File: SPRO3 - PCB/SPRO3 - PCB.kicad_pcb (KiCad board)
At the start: 2 copper layers, 100 x 100 mm, 39 parts, among them J1 Power Input, J10 Conn_01x03_Pin, J11 Conn_01x03_Pin, J12 Conn_01x03_Pin, J13 Conn_01x03_Pin, J14 Conn_01x03_Pin, J15 Conn_01x03_Pin, J16 Spare I2C PINS, J2 2nd PCB, J3 Servo Motor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

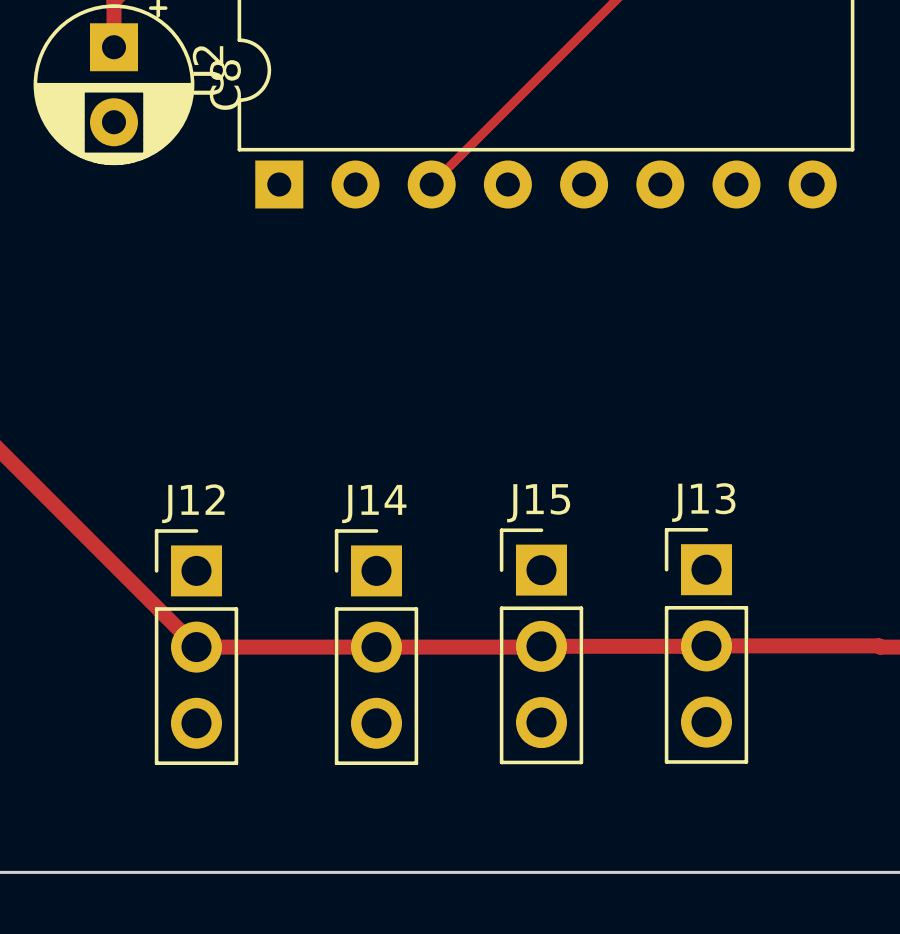
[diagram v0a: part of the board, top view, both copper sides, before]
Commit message: First attempt at designing the board for the second PCB
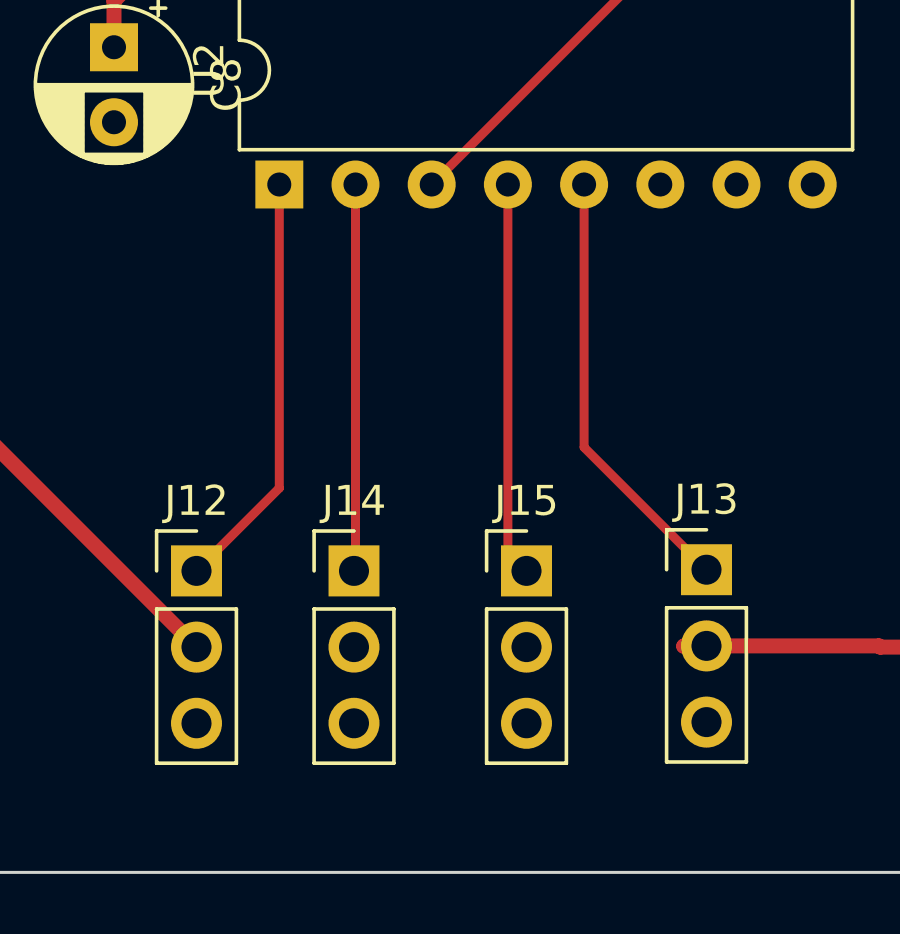
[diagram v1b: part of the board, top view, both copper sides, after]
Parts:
- moved J14 0.75 mm to (90.2, 140.2)
- moved J15 0.50 mm to (96.0, 140.2)
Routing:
- net +5V: track 253.2 -> 236.9 mm
- net Net-(J13-Pin_1): track 0.00 -> 14.5 mm
- net Net-(J12-Pin_1): track 0.00 -> 14.0 mm
- net Net-(J15-Pin_1): track 0.00 -> 13.1 mm
- net Net-(J14-Pin_1): track 0.00 -> 12.9 mm
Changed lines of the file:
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@@
 		(tags "CP Radial series Radial pin pitch 2.50mm  diameter 5mm Electrolytic Capacitor")
 		(property "Reference" "C5"
-			(at 1.25 -3.75 360)
+			(at 1.25 -3.75 0)
 			(layer "F.SilkS")
 			(effects
@@
 		)
 		(property "Value" "0.1uF"
-			(at 1.25 3.75 360)
+			(at 1.25 3.75 0)
 			(layer "F.Fab")
 			(effects
@@
 		)
 		(fp_text user "${REFERENCE}"
-			(at 1.25 0 360)
+			(at 1.25 0 0)
 			(layer "F.Fab")
 			(effects
@@
 		)
 		(fp_text user "${REFERENCE}"
-			(at 0 2.54 360)
+			(at 0 2.54 0)
 			(layer "F.Fab")
 			(effects
@@
 		(tags "Through hole pin header THT 1x03 2.54mm single row")
 		(property "Reference" "J13"
-			(at 0 -2.33 360)
+			(at 0 -2.33 0)
 			(layer "F.SilkS")
 			(effects
@@
 		)
 		(property "Value" "Conn_01x03_Pin"
-			(at 0 7.41 360)
+			(at 0 7.41 0)
 			(layer "F.Fab")
 			(effects
@@
 		(tags "terminal block bornier2")
 		(property "Reference" "J1"
-			(at 2.54 -5.08 360)
+			(at 2.54 -5.08 0)
 			(layer "F.SilkS")
 			(effects
@@
 		)
 		(property "Value" "Power Input"
-			(at 2.54 5.08 360)
+			(at 2.54 5.08 0)
 			(layer "F.Fab")
 			(effects
@@
 		)
 		(fp_text user "${REFERENCE}"
-			(at 2.54 0 360)
+			(at 2.54 0 0)
 			(layer "F.Fab")
 			(effects
@@
 		)
 		(fp_text user "${REFERENCE}"
-			(at 0 3.81 360)
+			(at 0 3.81 0)
 			(layer "F.Fab")
 			(effects
@@
 		(tags "THT DIP DIL PDIP 2.54mm 7.62mm 300mil")
 		(property "Reference" "U1"
-			(at 3.81 -2.33 360)
+			(at 3.81 -2.33 0)
 			(layer "F.SilkS")
 			(effects
@@
 		)
 		(property "Value" "~"
-			(at 3.81 9.95 360)
+			(at 3.81 9.95 0)
 			(layer "F.Fab")
 			(effects
@@
 		)
 		(fp_text user "${REFERENCE}"
-			(at 3.81 3.81 360)
+			(at 3.81 3.81 0)
 			(layer "F.Fab")
 			(effects
@@
 		)
 		(fp_text user "${REFERENCE}"
-			(at 0 3.81 360)
+			(at 0 3.81 0)
 			(layer "F.Fab")
 			(effects
@@
 		(tags "Through hole pin header THT 1x03 2.54mm single row")
 		(property "Reference" "J12"
-			(at 0 -2.33 360)
+			(at 0 -2.33 0)
 			(layer "F.SilkS")
 			(effects
@@
 		)
 		(property "Value" "Conn_01x03_Pin"
-			(at 0 7.41 360)
+			(at 0 7.41 0)
 			(layer "F.Fab")
 			(effects
@@
 	(footprint "Connector_PinHeader_2.54mm:PinHeader_1x03_P2.54mm_Vertical"
 		(layer "F.Cu")
-		(at 91 140.25)
+		(at 90.25 140.25)
 		(descr "Through hole straight pin header, 1x03, 2.54mm pitch, single row")
 		(tags "Through hole pin header THT 1x03 2.54mm single row")
 		(property "Reference" "J14"
-			(at 0 -2.33 360)
+			(at 0 -2.33 0)
 			(layer "F.SilkS")
 			(effects
@@
 		)
 		(property "Value" "Conn_01x03_Pin"
-			(at 0 7.41 360)
+			(at 0 7.41 0)
 			(layer "F.Fab")
 			(effects
@@
 		)
 		(fp_text user "${REFERENCE}"
-			(at 0 2.54 360)
+			(at 0 2.54 0)
 			(layer "F.Fab")
 			(effects
@@
 		(tags "Through hole pin header THT 1x06 2.54mm single row")
 		(property "Reference" "J4"
-			(at 0 -2.33 360)
+			(at 0 -2.33 0)
 			(layer "F.SilkS")
 			(effects
@@
 		)
 		(property "Value" "L298N Module"
-			(at 0 15.03 360)
+			(at 0 15.03 0)
 			(layer "F.Fab")
 			(effects
@@
 		)
 		(fp_text user "${REFERENCE}"
-			(at 0 2.54 360)
+			(at 0 2.54 0)
 			(layer "F.Fab")
 			(effects
@@
 		(tags "LED diameter 5.0mm 2 pins")
 		(property "Reference" "D2"
-			(at 1.27 -3.96 360)
+			(at 1.27 -3.96 0)
 			(layer "F.SilkS")
 			(effects
@@
 		)
 		(property "Value" "LED"
-			(at 1.27 3.96 360)
+			(at 1.27 3.96 0)
 			(layer "F.Fab")
 			(effects
@@
 		)
 		(fp_text user "${REFERENCE}"
-			(at 1.25 0 360)
+			(at 1.25 0 0)
 			(layer "F.Fab")
 			(effects
@@
 		)
 		(fp_text user "${REFERENCE}"
-			(at 0 3.81 360)
+			(at 0 3.81 0)
 			(layer "F.Fab")
 			(effects
@@
 		)
 		(fp_text user "${REFERENCE}"
-			(at 0 2.54 360)
+			(at 0 2.54 0)
 			(layer "F.Fab")
 			(effects
@@
 	(footprint "Connector_PinHeader_2.54mm:PinHeader_1x03_P2.54mm_Vertical"
 		(layer "F.Cu")
-		(at 96.5 140.225)
+		(at 96 140.25)
 		(descr "Through hole straight pin header, 1x03, 2.54mm pitch, single row")
 		(tags "Through hole pin header THT 1x03 2.54mm single row")
 		(property "Reference" "J15"
-			(at 0 -2.33 360)
+			(at 0 -2.33 0)
 			(layer "F.SilkS")
 			(effects
@@
 		)
 		(property "Value" "Conn_01x03_Pin"
-			(at 0 7.41 360)
+			(at 0 7.41 0)
 			(layer "F.Fab")
 			(effects
@@
 		)
 		(fp_text user "${REFERENCE}"
-			(at 0 2.54 360)
+			(at 0 2.54 0)
 			(layer "F.Fab")
 			(effects
@@
 		(tags "Through hole pin header THT 1x02 2.54mm single row")
 		(property "Reference" "J2"
-			(at 0 -2.33 360)
+			(at 0 -2.33 0)
 			(layer "F.SilkS")
 			(effects
@@
 		)
 		(property "Value" "2nd PCB"
-			(at 0 4.87 360)
+			(at 0 4.87 0)
 			(layer "F.Fab")
 			(effects
@@
 		(tags "Through hole pin header THT 1x03 2.54mm single row")
 		(property "Reference" "J3"
-			(at 0 -2.33 360)
+			(at 0 -2.33 0)
 			(layer "F.SilkS")
 			(effects
@@
 		)
 		(property "Value" "Servo Motor"
-			(at 0 7.41 360)
+			(at 0 7.41 0)
 			(layer "F.Fab")
 			(effects
@@
 	)
 	(segment
-		(start 96.485 142.765)
-		(end 96.46 142.79)
-		(width 0.5)
-		(layer "F.Cu")
-		(net 18)
-	)
-	(segment
 		(start 102 142.75)
 		(end 101.25 142.75)
@@
 	)
 	(segment
-		(start 101.235 142.765)
-		(end 96.5 142.765)
-		(width 0.5)
-		(layer "F.Cu")
-		(net 18)
-	)
-	(segment
 		(start 82.25 121.25)
 		(end 83.75 119.75)
@@
 	)
 	(segment
-		(start 91 142.79)
-		(end 85 142.79)
-		(width 0.5)
-		(layer "F.Cu")
-		(net 18)
-	)
-	(segment
-		(start 96.46 142.79)
-		(end 91 142.79)
-		(width 0.5)
-		(layer "F.Cu")
-		(net 18)
-	)
-	(segment
 		(start 164.07 94.75)
 		(end 159.21 89.89)
@@
 	)
 	(segment
-		(start 96.5 142.765)
-		(end 96.485 142.765)
-		(width 0.5)
-		(layer "F.Cu")
-		(net 18)
-	)
-	(segment
 		(start 164.12 94.8)
 		(end 164.07 94.75)
@@
 		(net 43)
 	)
+	(segment
+		(start 87.76 137.49)
+		(end 85 140.25)
+		(width 0.3)
+		(layer "F.Cu")
+		(net 44)
+	)
+	(segment
+		(start 87.76 127.37)
+		(end 87.76 137.49)
+		(width 0.3)
+		(layer "F.Cu")
+		(net 44)
+	)
+	(segment
+		(start 97.92 136.13)
+		(end 102 140.21)
+		(width 0.3)
+		(layer "F.Cu")
+		(net 45)
+	)
+	(segment
+		(start 97.92 127.37)
+		(end 97.92 136.13)
+		(width 0.3)
+		(layer "F.Cu")
+		(net 45)
+	)
+	(segment
+		(start 90.3 127.37)
+		(end 90.3 140.2)
+		(width 0.3)
+		(layer "F.Cu")
+		(net 46)
+	)
+	(segment
+		(start 90.3 140.2)
+		(end 90.25 140.25)
+		(width 0.3)
+		(layer "F.Cu")
+		(net 46)
+	)
+	(segment
+		(start 95.38 139.63)
+		(end 96 140.25)
+		(width 0.3)
+		(layer "F.Cu")
+		(net 47)
+	)
+	(segment
+		(start 95.38 127.37)
+		(end 95.38 139.63)
+		(width 0.3)
+		(layer "F.Cu")
+		(net 47)
+	)
 )

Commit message: First attempt at designing the main PCB board
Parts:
- removed J16: Spare I2C PINS, Connector_PinHeader_2.54mm:PinHeader_1x04_P2.54mm_Vertical
- moved C10 135.8 mm to (93.5, 132.0), turned to 180 degrees
- moved R2 121.8 mm to (133.9, 136.2)
- moved R1 117.8 mm to (136.6, 129.0), turned to 180 degrees
- moved R3 111.3 mm to (141.7, 132.5)
- moved C6 106.4 mm to (116.0, 133.5), turned to 90 degrees
- moved C2 103.1 mm to (93.0, 93.2)
- moved R5 86.8 mm to (157.5, 114.2), turned to -90 degrees
- moved C3 80.3 mm to (146.8, 126.8)
- moved C9 73.8 mm to (153.0, 108.2), turned to 180 degrees
- moved C1 73.2 mm to (128.2, 133.5), turned to -90 degrees
- moved C11 71.8 mm to (153.0, 92.5)
- moved TH1 67.5 mm to (136.5, 132.5), turned to 180 degrees
- moved C7 48.8 mm to (250.8, 116.8)
- moved R4 46.2 mm to (92.9, 98.5)
- moved SW1 45.0 mm to (113.0, 82.0), turned to 180 degrees
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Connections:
- A1 pad 19: /IN2 -> /NTC_Vout(ADC3)
- A1 pad 22: /NTC_Vout(ADC3) -> /IN2
- J4 pad 2: /IN1 -> /OC0B
- J4 pad 3: /IN2 -> /IN1
- J4 pad 6: /OC0B -> /IN2
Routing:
- net Net-(U1--): track 0.00 -> 37.0 mm
- net /IN1: track 0.00 -> 33.0 mm
- net /ADC7: track 33.4 -> 5.68 mm
- net /IN4: track 0.00 -> 27.4 mm
- net /IN3: track 0.00 -> 27.4 mm
- net /IN2: track 0.00 -> 27.4 mm
- net +5V: track 236.9 -> 214.5 mm
- net /NTC_Vout(ADC3): track 0.00 -> 22.4 mm
- net Net-(J11-Pin_1): track 32.9 -> 10.8 mm
- net /SCL: track 35.9 -> 14.2 mm
- net /SDA: track 36.5 -> 18.8 mm
- net Net-(J8-Pin_1): track 26.9 -> 10.2 mm
- net Net-(U1-+): track 0.00 -> 12.6 mm
- net /ADC6: track 25.3 -> 13.0 mm
- net Net-(J9-Pin_1): track 21.9 -> 9.74 mm
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
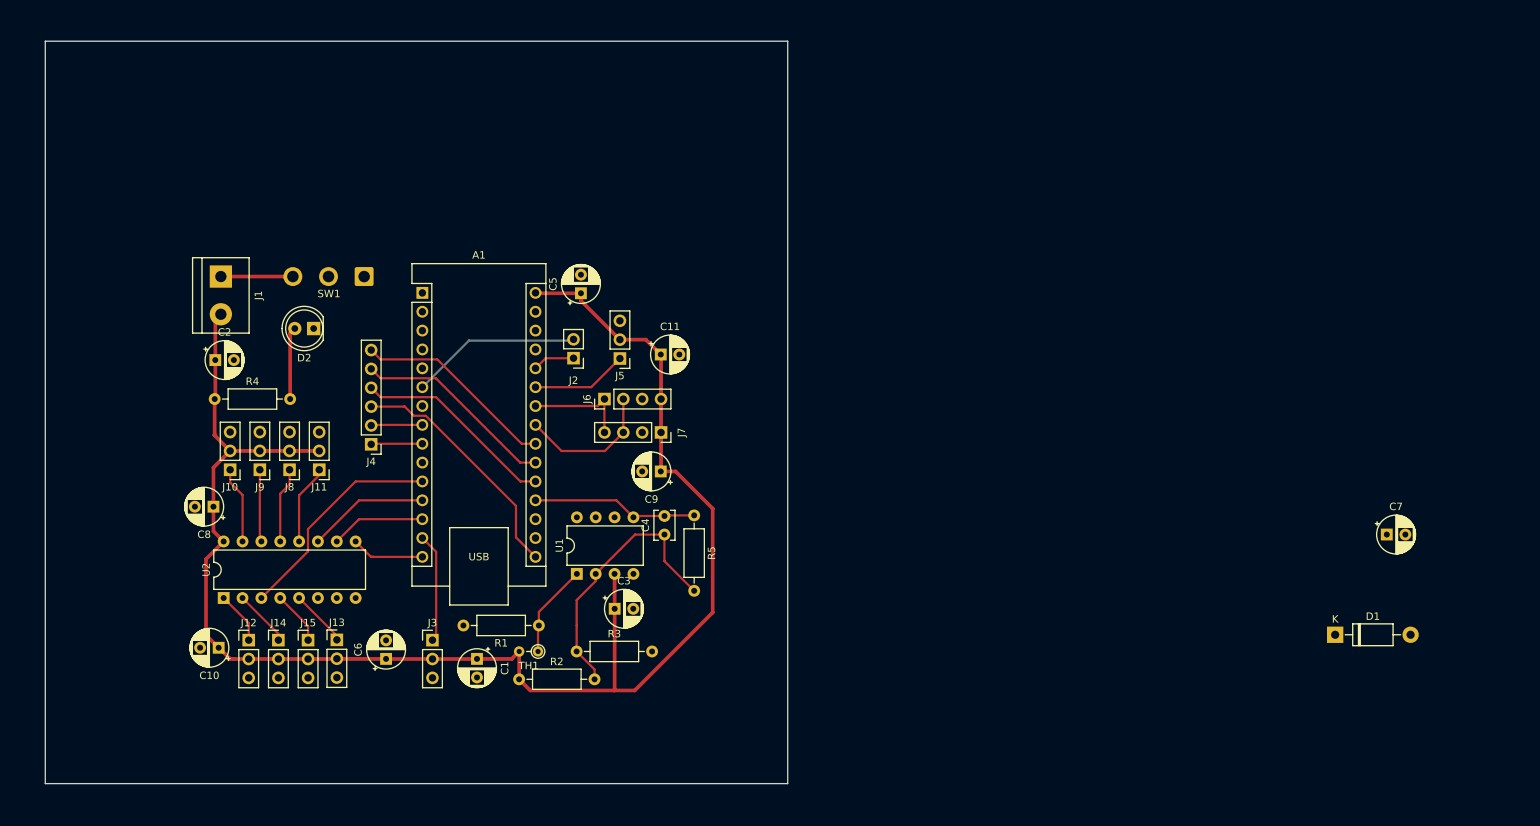
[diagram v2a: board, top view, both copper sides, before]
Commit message: Made some edits to the main PCB board
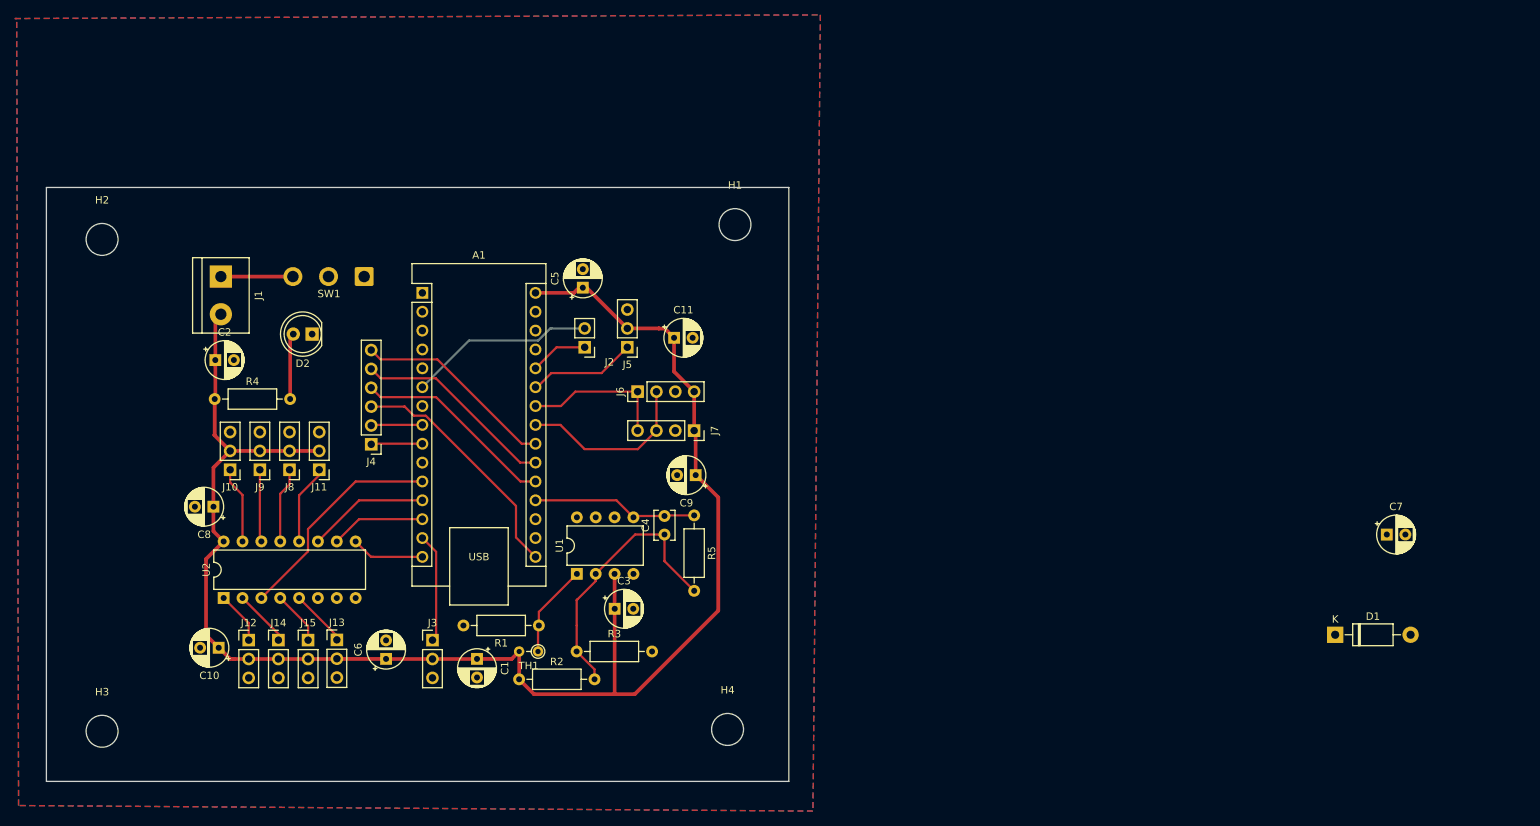
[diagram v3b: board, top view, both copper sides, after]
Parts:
- added H1: MountingHole, MountingHole:MountingHole_4.3mm_M4, F.Cu at (163.0, 75.0)
- added H2: MountingHole, MountingHole:MountingHole_4.3mm_M4, F.Cu at (77.8, 77.0)
- added H3: MountingHole, MountingHole:MountingHole_4.3mm_M4, F.Cu at (77.8, 143.2)
- added H4: MountingHole, MountingHole:MountingHole_4.3mm_M4, F.Cu at (162.0, 143.0)
- moved C9 4.73 mm to (157.7, 108.8)
- moved J6 4.57 mm to (149.9, 97.5)
- moved J7 4.47 mm to (157.5, 102.8)
- moved C11 2.88 mm to (154.8, 90.2)
- moved J2 2.10 mm to (142.8, 91.5)
- moved J5 1.82 mm to (148.5, 91.5)
- moved C5 0.79 mm to (142.5, 83.5)
- moved D2 0.78 mm to (106.0, 89.8)
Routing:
- net /SCL: track 14.2 -> 19.8 mm
- net /SDA: track 18.8 -> 23.9 mm
- net +5V: track 214.5 -> 217.4 mm
- net /OC2B: track 23.0 -> 25.1 mm
- net /ADC7: track 5.68 -> 7.79 mm
- net /ADC6: track 13.0 -> 14.6 mm
- net Net-(D2-A): track 9.76 -> 8.92 mm
- added copper zone on B.Cu, net GND
- added copper zone on F.Cu, net GND
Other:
- board size 100 x 100 mm -> 100 x 80 mm

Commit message: Added to main PCB board
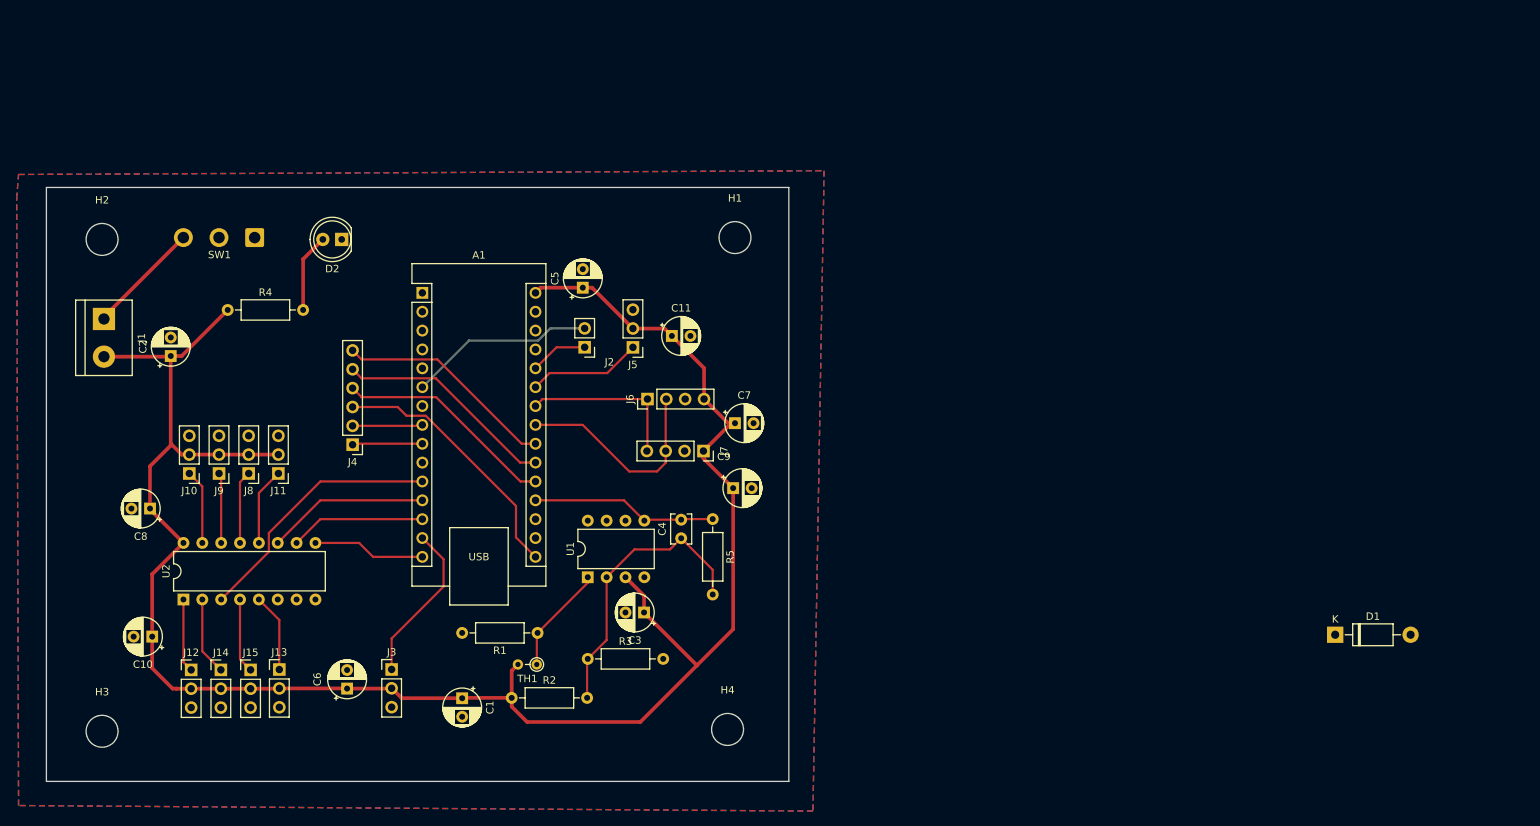
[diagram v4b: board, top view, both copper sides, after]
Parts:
- moved C7 89.1 mm to (163.0, 101.8)
- moved J1 16.8 mm to (78.0, 87.7)
- moved SW1 15.7 mm to (98.3, 76.8)
- moved D2 13.4 mm to (110.0, 77.0)
- moved R4 12.1 mm to (94.7, 86.5)
- moved C10 9.08 mm to (84.5, 130.5)
- moved J12 8.72 mm to (89.8, 135.0)
- moved J13 8.72 mm to (101.6, 134.9)
- moved J14 8.72 mm to (93.8, 135.0)
- moved J15 8.72 mm to (97.8, 135.0)
- moved C8 8.55 mm to (84.2, 113.2)
- moved J3 6.77 mm to (116.8, 134.9)
- moved C6 6.60 mm to (110.8, 137.5)
- moved C2 6.02 mm to (87.0, 92.7), turned to 90 degrees
- moved C1 5.66 mm to (126.2, 138.8)
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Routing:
- net +5V: track 217.4 -> 257.8 mm
- net /OC2A: track 14.7 -> 22.5 mm
- net Net-(J1-Pin_1): track 9.70 -> 15.4 mm
- net /A: track 16.4 -> 21.9 mm
- net /B: track 12.8 -> 18.3 mm
- net /C: track 9.85 -> 15.2 mm
- net /SDA: track 23.9 -> 29.2 mm
- net /Echo&Trig: track 29.9 -> 35.2 mm
- net Net-(J12-Pin_1): track 7.07 -> 9.91 mm
- net Net-(J13-Pin_1): track 7.74 -> 10.6 mm
- net Net-(J14-Pin_1): track 7.75 -> 10.5 mm
- net /SCL: track 19.8 -> 22.5 mm
- net /NTC_Vout(ADC3): track 22.4 -> 25.1 mm
- net /OC0A: track 6.92 -> 9.45 mm
- net /OC0B: track 6.92 -> 9.45 mm
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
